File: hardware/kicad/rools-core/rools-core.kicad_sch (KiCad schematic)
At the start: 0 parts

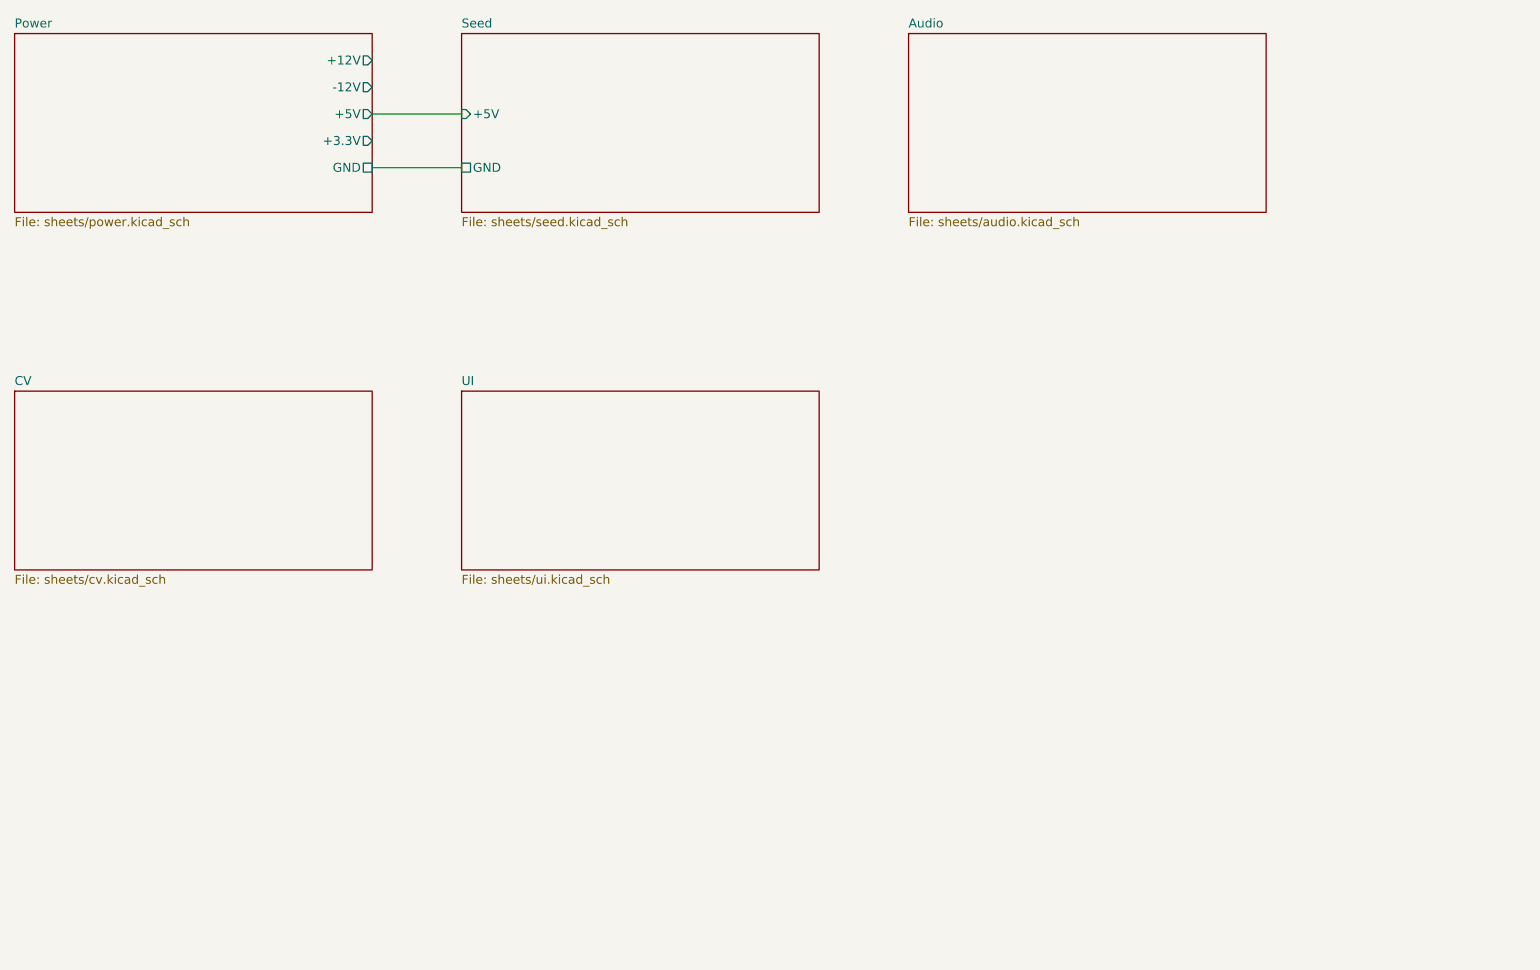
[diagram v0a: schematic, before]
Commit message: Wire rools-core KiCad sheets with global labels and UI peripherals.
Migrate inter-sheet nets to global labels and flesh out UI, power, and
child-sheet power entry so net names align with pins.h for PCB routing.

Co-authored-by: Cursor <cursoragent@cursor.com>
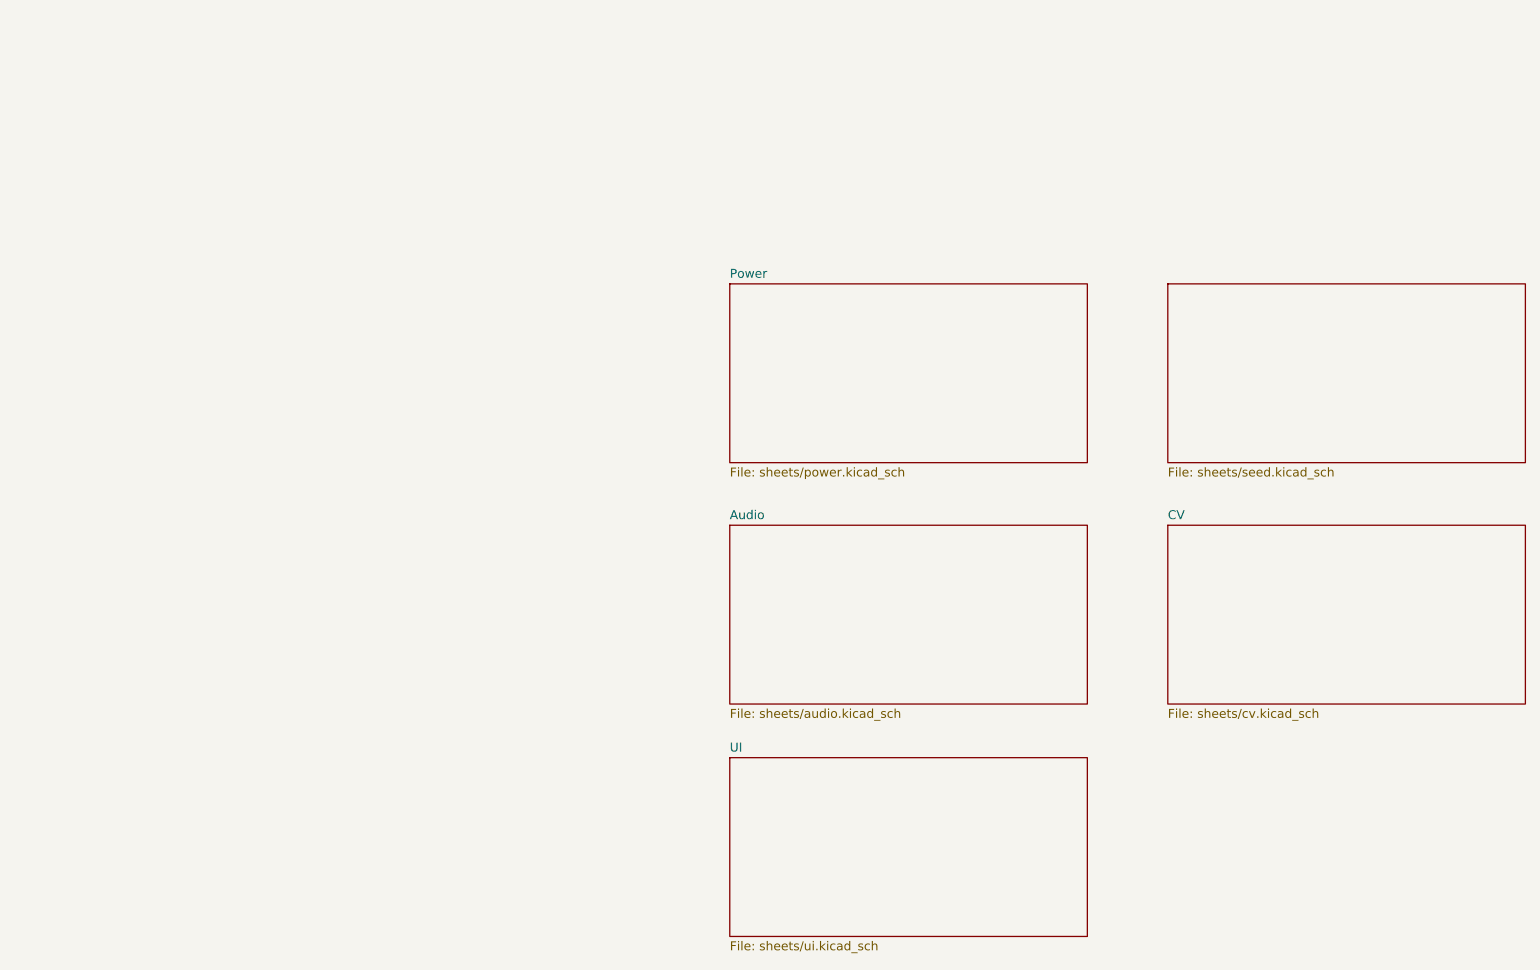
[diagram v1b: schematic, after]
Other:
- sheet Power ports: added none; removed +12V, +3.3V, +5V, -12V, GND
- sheet Seed ports: added none; removed +5V, GND
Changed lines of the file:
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@@
 		(title "Rools Core 10HP")
 		(date "2026-06-14")
-		(rev "0.1")
+		(rev "0.2")
 		(company "Rools")
 		(comment 1 "Eurorack Core — 不含 Exp 2HP")
 	)
-	(wire
-		(pts
-			(xy 76.2 57.15) (xy 88.9 57.15)
-		)
-		(stroke
-			(width 0)
-			(type default)
-		)
-	)
-	(wire
-		(pts
-			(xy 76.2 49.53) (xy 88.9 49.53)
-		)
-		(stroke
-			(width 0)
-			(type default)
-		)
-	)
 	(sheet
-		(at 88.9 38.1)
+		(at 189.23 73.66)
 		(size 50.8 25.4)
 		(exclude_from_sim no)
@@
 		)
 		(property "Sheetname" "Seed"
-			(at 88.9 37.3886 0)
+			(at 189.23 72.9486 0)
+			(hide yes)
 			(show_name no)
 			(do_not_autoplace no)
@@
 		)
 		(property "Sheetfile" "sheets/seed.kicad_sch"
-			(at 88.9 64.1344 0)
+			(at 189.23 99.6944 0)
 			(show_name no)
 			(do_not_autoplace no)
@@
 			)
 		)
-		(pin "+5V" input
-			(at 88.9 49.53 180)
-			(effects
-				(font
-					(size 1.27 1.27)
-				)
-				(justify left)
-			)
-		)
-		(pin "GND" passive
-			(at 88.9 57.15 180)
-			(effects
-				(font
-					(size 1.27 1.27)
-				)
-				(justify left)
-			)
-		)
 	)
 	(sheet
-		(at 25.4 38.1)
+		(at 127 73.66)
 		(size 50.8 25.4)
 		(exclude_from_sim no)
@@
 		)
 		(property "Sheetname" "Power"
-			(at 25.4 37.3886 0)
+			(at 127 72.9486 0)
 			(show_name no)
 			(do_not_autoplace no)
@@
 		)
 		(property "Sheetfile" "sheets/power.kicad_sch"
-			(at 25.4 64.1344 0)
+			(at 127 99.6944 0)
 			(show_name no)
 			(do_not_autoplace no)
@@
 			)
 		)
-		(pin "+12V" output
-			(at 76.2 41.91 0)
-			(effects
-				(font
-					(size 1.27 1.27)
-				)
-				(justify right)
-			)
-		)
-		(pin "-12V" output
-			(at 76.2 45.72 0)
-			(effects
-				(font
-					(size 1.27 1.27)
-				)
-				(justify right)
-			)
-		)
-		(pin "+5V" output
-			(at 76.2 49.53 0)
-			(effects
-				(font
-					(size 1.27 1.27)
-				)
-				(justify right)
-			)
-		)
-		(pin "+3.3V" output
-			(at 76.2 53.34 0)
-			(effects
-				(font
-					(size 1.27 1.27)
-				)
-				(justify right)
-			)
-		)
-		(pin "GND" passive
-			(at 76.2 57.15 0)
-			(effects
-				(font
-					(size 1.27 1.27)
-				)
-				(justify right)
-			)
-		)
 	)
 	(sheet
-		(at 25.4 88.9)
+		(at 189.23 107.95)
 		(size 50.8 25.4)
 		(exclude_from_sim no)
@@
 		)
 		(property "Sheetname" "CV"
-			(at 25.4 88.1886 0)
+			(at 189.23 107.2386 0)
 			(show_name no)
 			(do_not_autoplace no)
@@
 		)
 		(property "Sheetfile" "sheets/cv.kicad_sch"
-			(at 25.4 114.9344 0)
+			(at 189.23 133.9844 0)
 			(show_name no)
 			(do_not_autoplace no)
@@
 	)
 	(sheet
-		(at 152.4 38.1)
+		(at 127 107.95)
 		(size 50.8 25.4)
 		(exclude_from_sim no)
@@
 		)
 		(property "Sheetname" "Audio"
-			(at 152.4 37.3886 0)
+			(at 127 107.2386 0)
 			(show_name no)
 			(do_not_autoplace no)
@@
 		)
 		(property "Sheetfile" "sheets/audio.kicad_sch"
-			(at 152.4 64.1344 0)
+			(at 127 133.9844 0)
 			(show_name no)
 			(do_not_autoplace no)
@@
 	)
 	(sheet
-		(at 88.9 88.9)
+		(at 127 140.97)
 		(size 50.8 25.4)
 		(exclude_from_sim no)
@@
 		)
 		(property "Sheetname" "UI"
-			(at 88.9 88.1886 0)
+			(at 127 140.2586 0)
 			(show_name no)
 			(do_not_autoplace no)
@@
 		)
 		(property "Sheetfile" "sheets/ui.kicad_sch"
-			(at 88.9 114.9344 0)
+			(at 127 167.0044 0)
 			(show_name no)
 			(do_not_autoplace no)

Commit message: Add QSPI settings persistence, CV calibration app, and CV output driver.
Co-authored-by: Cursor <cursoragent@cursor.com>
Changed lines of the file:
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@@
 		(property "Sheetname" "Seed"
 			(at 189.23 72.9486 0)
-			(hide yes)
 			(show_name no)
 			(do_not_autoplace no)
@@
 			)
 		)
+		(instances
+			(project "rools-core"
+				(path "/e63e39d7-6ac0-4ffd-8aa3-1841a4541b55"
+					(page "1")
+				)
+			)
+		)
 	)
 	(sheet
@@
 		(on_board yes)
 		(dnp no)
-		(fields_autoplaced yes)
 		(stroke
 			(width 0.1524)
@@
 			)
 		)
+		(instances
+			(project "rools-core"
+				(path "/e63e39d7-6ac0-4ffd-8aa3-1841a4541b55"
+					(page "2")
+				)
+			)
+		)
 	)
 	(sheet
@@
 			)
 		)
+		(instances
+			(project "rools-core"
+				(path "/e63e39d7-6ac0-4ffd-8aa3-1841a4541b55"
+					(page "3")
+				)
+			)
+		)
 	)
 	(sheet
@@
 			)
 		)
+		(instances
+			(project "rools-core"
+				(path "/e63e39d7-6ac0-4ffd-8aa3-1841a4541b55"
+					(page "4")
+				)
+			)
+		)
 	)
 	(sheet
@@
 			)
 		)
+		(instances
+			(project "rools-core"
+				(path "/e63e39d7-6ac0-4ffd-8aa3-1841a4541b55"
+					(page "5")
+				)
+			)
+		)
